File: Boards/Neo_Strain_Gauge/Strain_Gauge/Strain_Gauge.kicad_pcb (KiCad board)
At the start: 2 copper layers, 85 x 56 mm, 60 parts, among them J1 Screw_Terminal_01x03, J2 Screw_Terminal_01x03, J3 Screw_Terminal_01x03, J4 Screw_Terminal_01x03, J5 Conn_01x02, J6 USB_B_Micro, J7 Conn_02x10_Counter_Clockwise, J8 Conn_02x12_Counter_Clockwise, U1 W25Q128JVS, U2 NCP1117-3.3_SOT223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

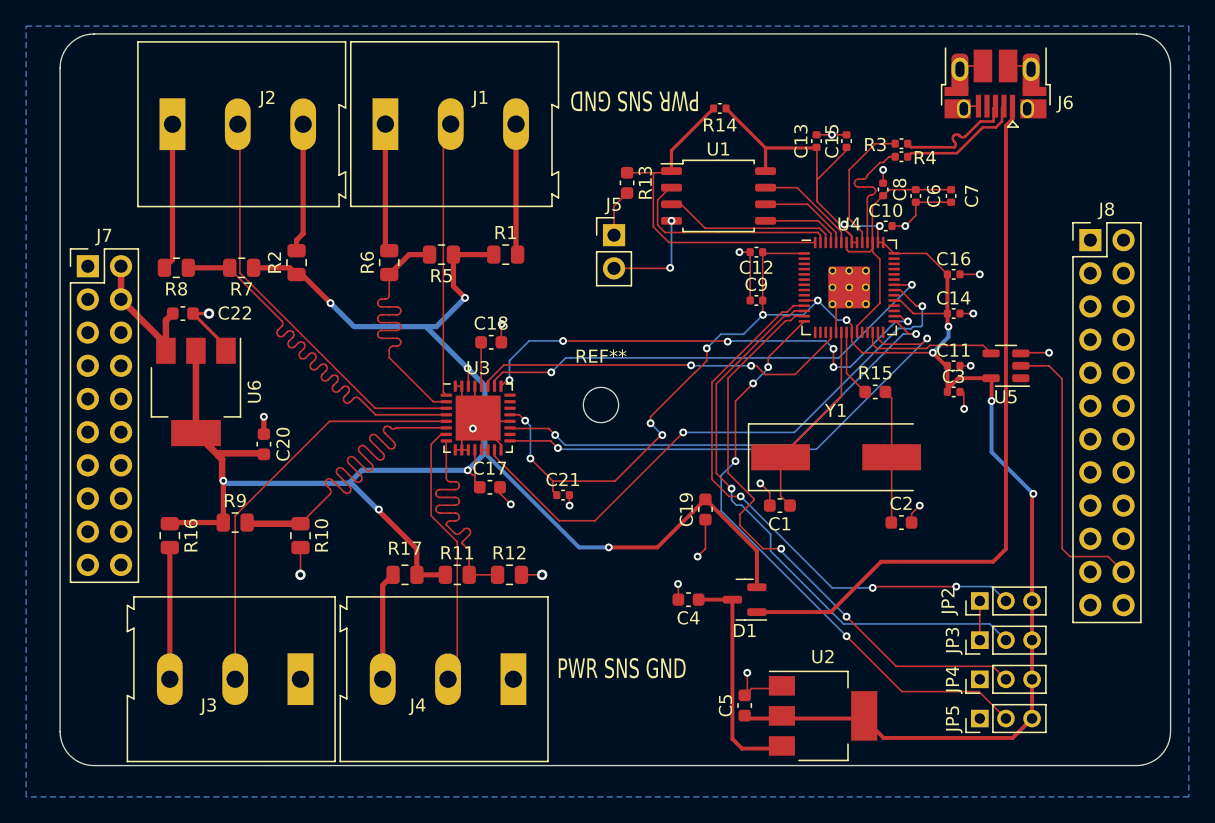
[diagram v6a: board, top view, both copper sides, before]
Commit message: More micro-adjustments and add the I2C lines
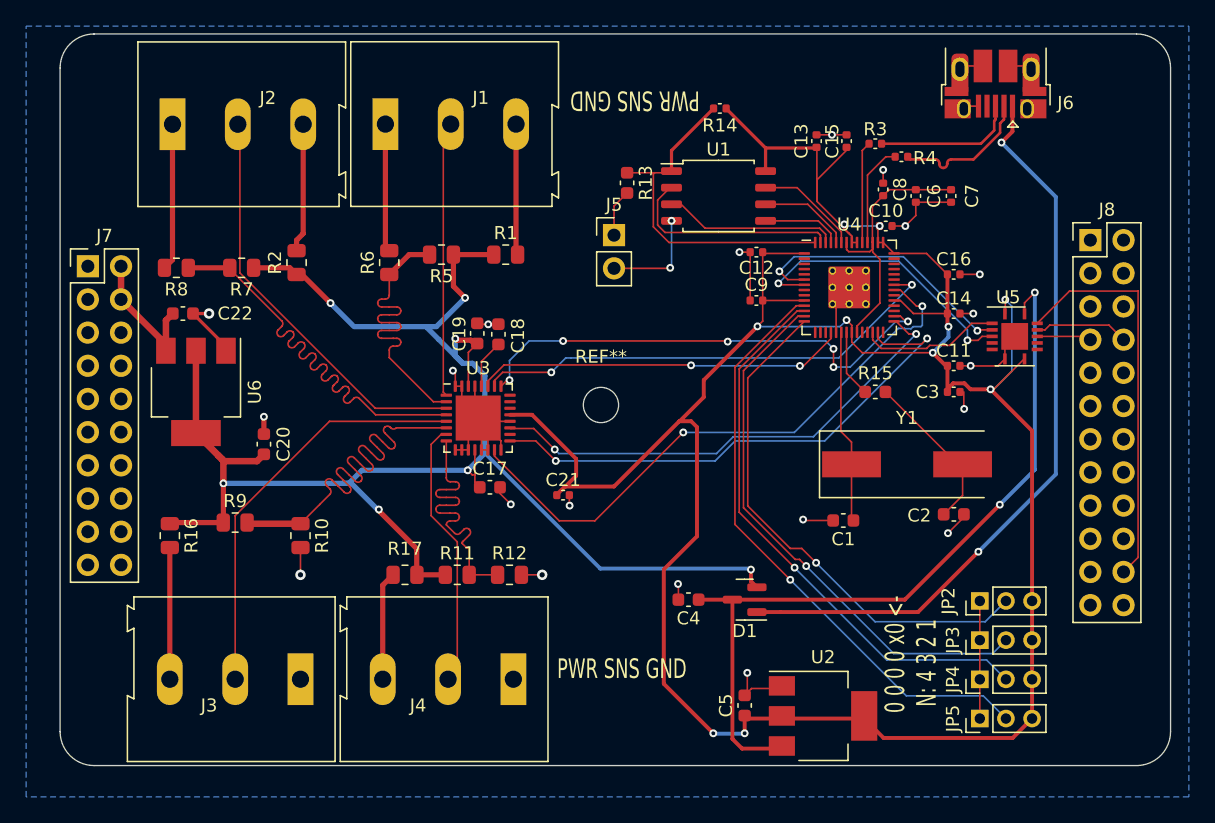
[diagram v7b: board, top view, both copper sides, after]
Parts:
- U5: value SN74LV1T34DBV -> TXB0104RGY; footprint Package_TO_SOT_SMD:SOT-23-5 -> Package_DFN_QFN:Texas_S-PVQFN-N14
- moved C19 22.1 mm to (132.5, 76.5), turned to -90 degrees
- moved Y1 5.46 mm to (165.4, 86.5)
- moved C1 4.98 mm to (160.6, 90.8)
- moved C2 4.06 mm to (169.0, 90.4)
- moved U5 2.35 mm to (173.7, 76.8), turned to 0 degrees
- moved R3 2.00 mm to (163.0, 62.0)
- moved C18 0.82 mm to (134.2, 76.6), turned to 90 degrees
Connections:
- JP2 pad 2: /GPIO8 -> /GPIO11
- JP3 pad 2: /GPIO9 -> /GPIO10
- JP4 pad 2: /GPIO10 -> /GPIO9
- JP5 pad 2: /GPIO11 -> /GPIO8
- U5 pad 1: unconnected-(U5-Pad1) -> +3V3
- U5 pad 2: /reset -> /RUN
- U5 pad 3: GND -> /GPIO4
- U5 pad 4: /RUN -> /GPIO5
- U5 pad 5: +3V3 -> unconnected-(U5-Pad5)
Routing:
- net +3V3: track 161.6 -> 205.8 mm, vias 14 -> 10
- net /REG_POWER: track 17.3 -> 60.1 mm, vias 0 -> 2
- net /GPIO5: track 0.00 -> 22.2 mm, vias 0 -> 2
- net /GPIO4: track 0.00 -> 21.3 mm, vias 0 -> 2
- net GND: track 106.4 -> 115.2 mm, vias 24 -> 22
- net /reset: track 22.0 -> 30.7 mm
- net /XIN: track 22.1 -> 14.8 mm
- net /scl: track 0.00 -> 7.22 mm
- net /GPIO11: track 45.5 -> 40.0 mm, vias 4 -> 1
- net /sda: track 0.00 -> 4.17 mm
- net /GPIO10: track 45.7 -> 42.0 mm, vias 2 -> 1
- net +5V: track 129.9 -> 132.9 mm
- net /GPIO8: track 43.4 -> 46.2 mm, vias 3 -> 1
- net /USB_DR+: track 10.3 -> 7.78 mm
- net Net-(C2-Pad1): track 10.2 -> 12.6 mm
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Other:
- board text added: "0 0 0 0 x0 <- N: 4 3 2 1"

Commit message: I can't stop making micro-changes and optimizations
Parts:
- moved C18 0.12 mm to (134.1, 76.5)
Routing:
- net +3V3: track 205.8 -> 208.4 mm
- net /vcc: track 0.00 -> 2.54 mm
- net GND: track 115.2 -> 116.8 mm
- net /GPIO19: track 37.6 -> 36.7 mm, vias 6 -> 4
